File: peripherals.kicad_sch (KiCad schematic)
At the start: 20 parts, among them J10 Cam 2, J11 Cam 3, J13 Servo, J2 Encoder, J9 Cam 1, Q2 NPN, Q3 NPN, Q4 NPN, Q5 NPN

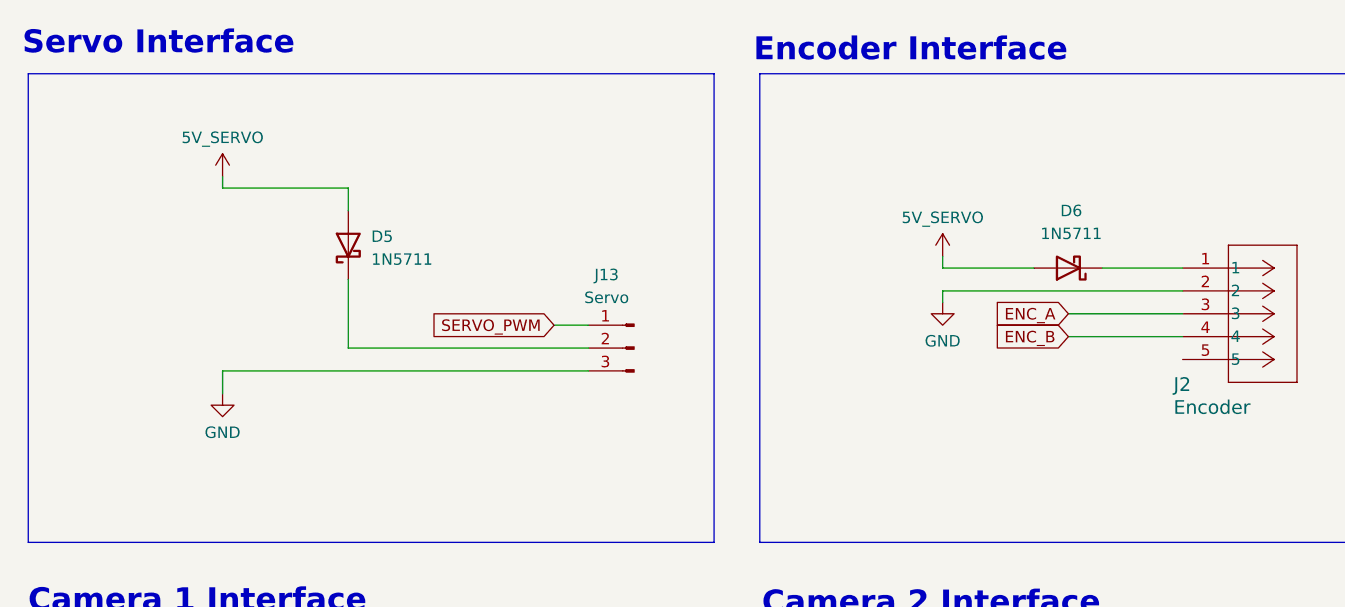
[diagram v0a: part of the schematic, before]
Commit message: remove schotkey diodes from servo and encoder interfaces
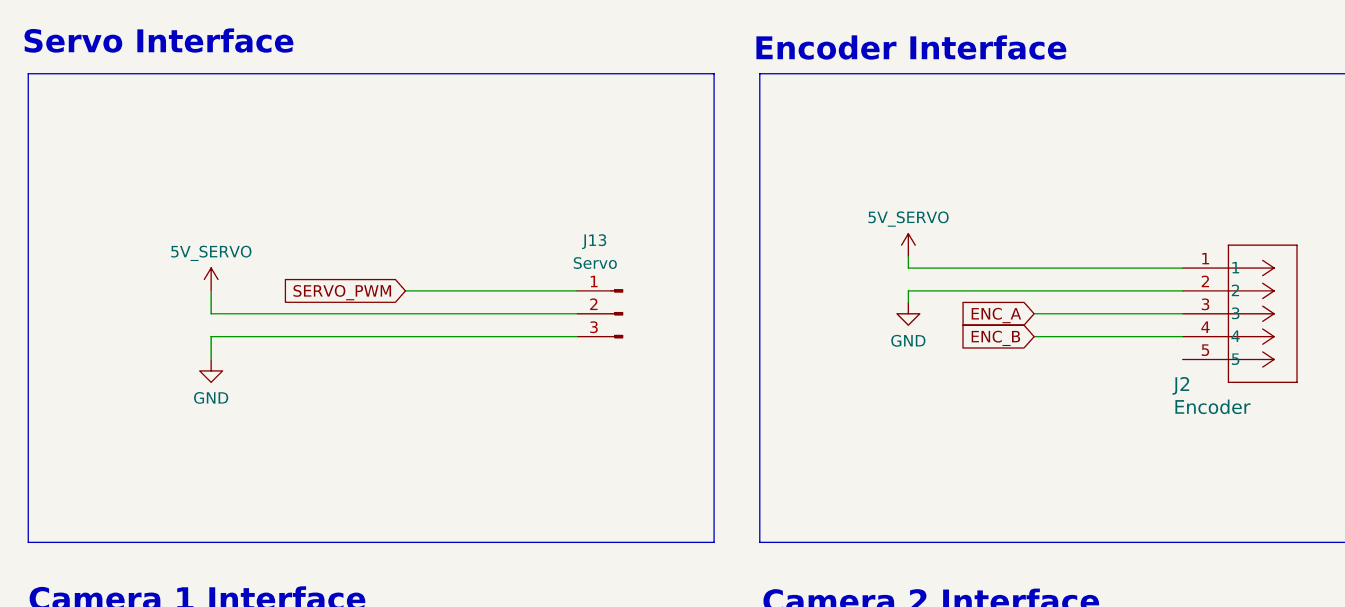
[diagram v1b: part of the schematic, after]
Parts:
- removed D5, D6: 1N5711, Diode_THT:D_DO-35_SOD27_P7.62mm_Horizontal, symbol Diode:1N5711
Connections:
- net 5V_SERVO: now also J13.2 (Pin_2), J2.1
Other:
- moved on the sheet: J13

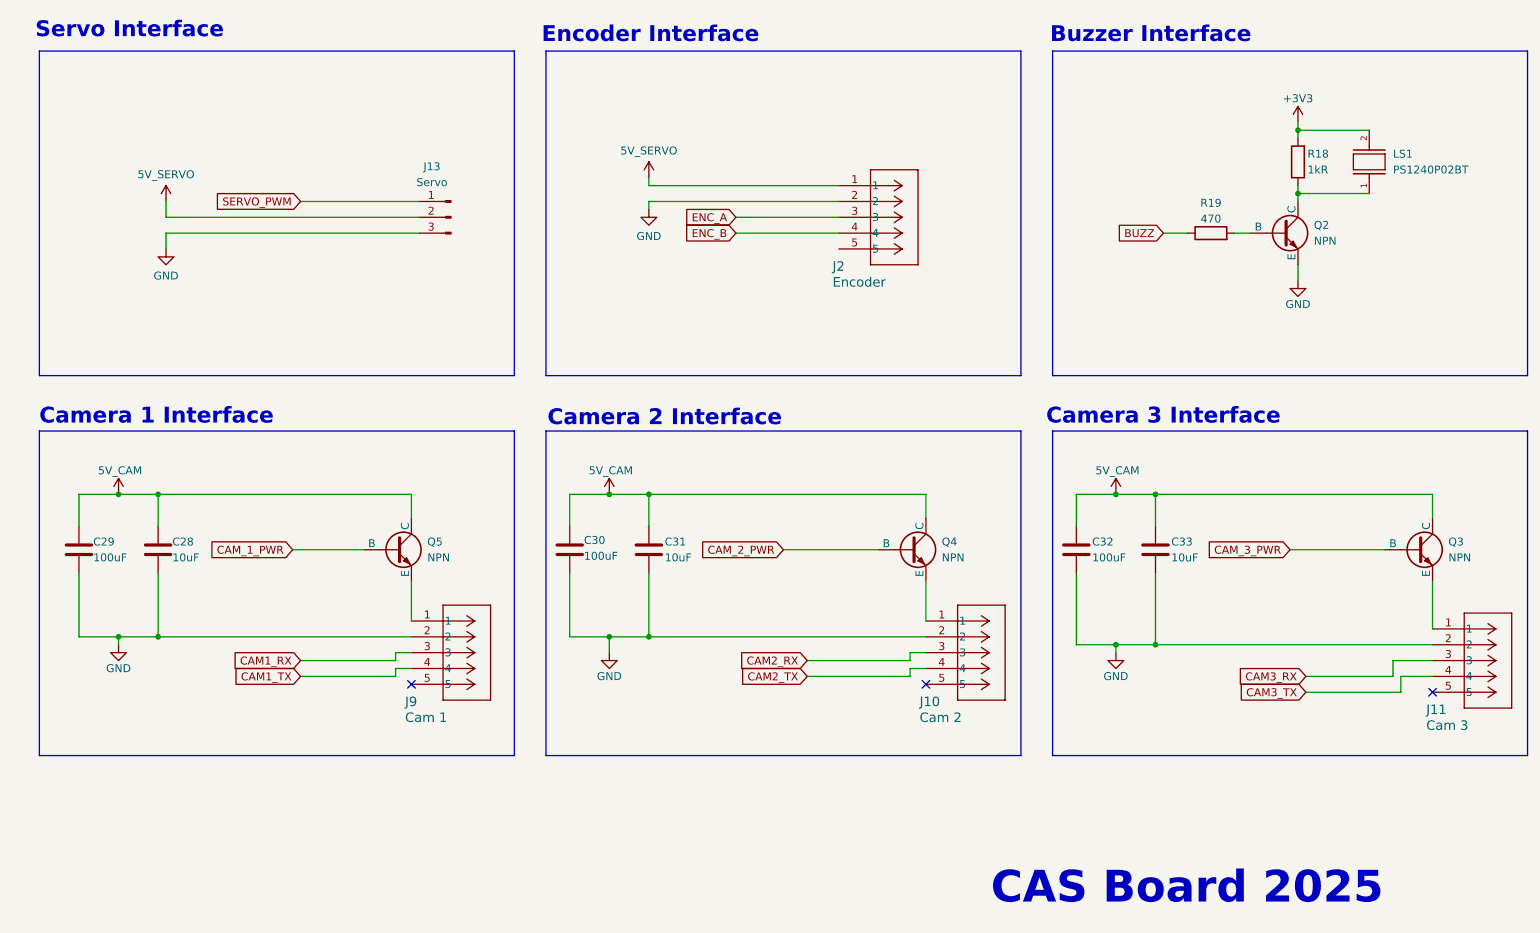
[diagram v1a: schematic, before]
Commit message: Redo footprints and add mosfet for camera power control
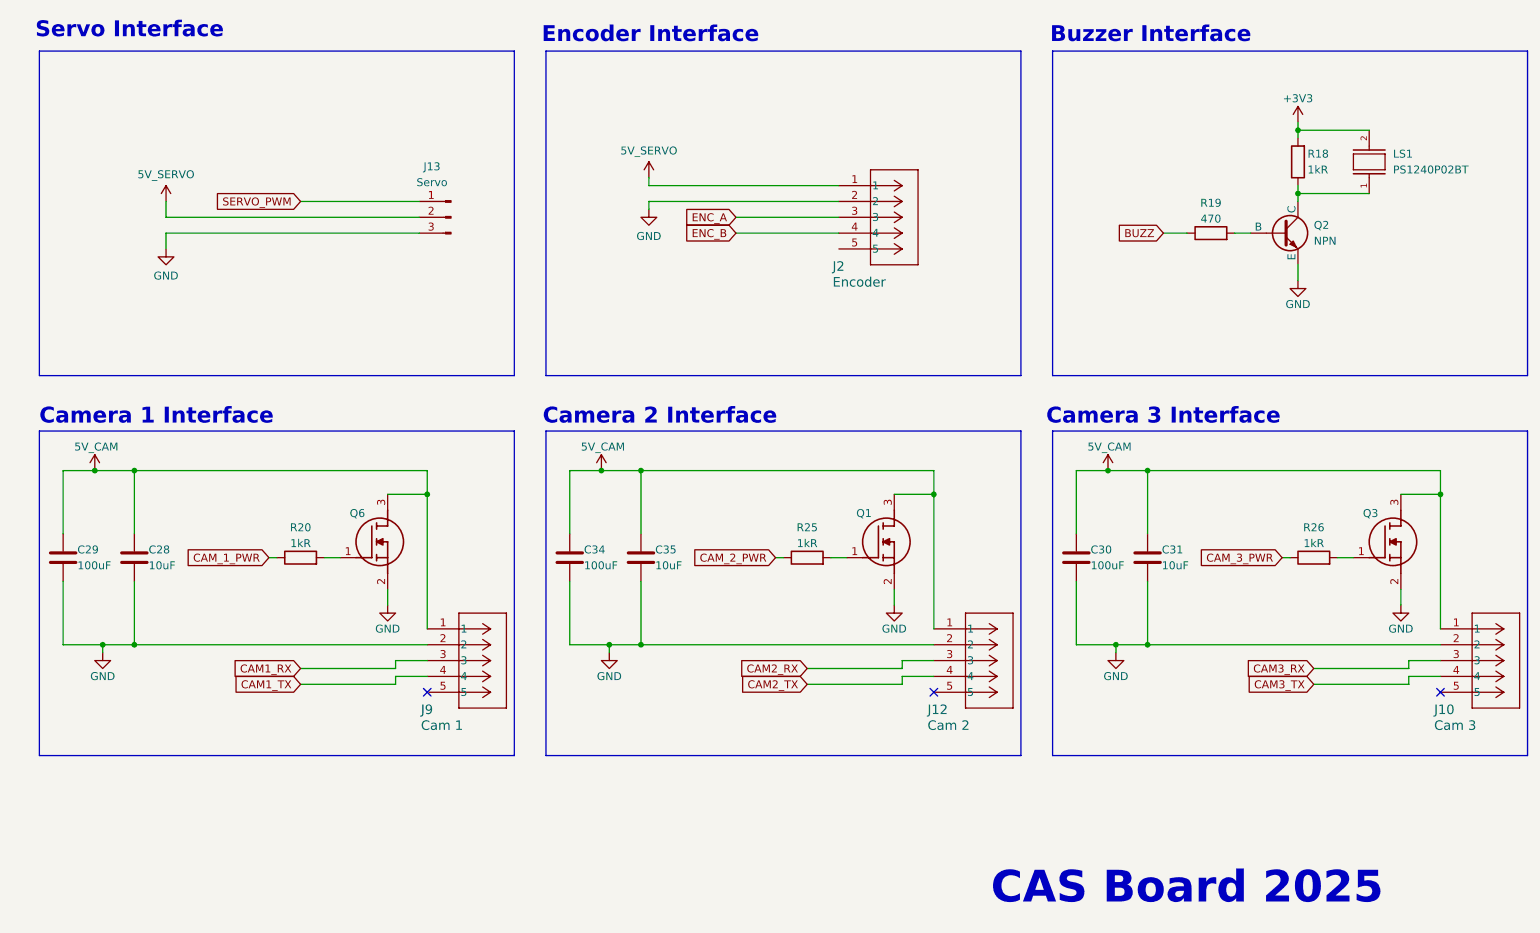
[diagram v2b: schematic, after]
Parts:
- removed C32: 100uF, Capacitor_SMD:C_0805_2012Metric_Pad1.18x1.45mm_HandSolder, symbol Device:C
- removed C33: 10uF, Capacitor_SMD:C_0805_2012Metric_Pad1.18x1.45mm_HandSolder, symbol Device:C
- removed J11: Cam 3, S05B_PASK_2_LF__SN_:CONN_S05B-PASK-2_JST, symbol 2025-06-21_05-21-07:S05B-PASK-2LFSN
- removed Q3, Q4, Q5: NPN, FSB560A:SSOT3_3X1P5_ONS, symbol Simulation_SPICE:NPN
- added C34: 100uF, Capacitor_SMD:C_0805_2012Metric_Pad1.18x1.45mm_HandSolder, symbol Device:C
- added C35: 10uF, Capacitor_SMD:C_0805_2012Metric_Pad1.18x1.45mm_HandSolder, symbol Device:C
- added J12: Cam 2, S05B_PASK_2_LF__SN_:CONN_S05B-PASK-2_JST, symbol 2025-06-21_05-21-07:S05B-PASK-2LFSN
- added Q1, Q3, Q6: BSS816NWH6327XTSA1, SOT65P210X100-3N, symbol BSS816NWH6327XTSA1:BSS816NWH6327XTSA1
- added R20, R25, R26: 1kR, Resistor_SMD:R_0805_2012Metric_Pad1.20x1.40mm_HandSolder, symbol Device:R
- J10: value Cam 2 -> Cam 3
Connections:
- net 5V_CAM: now also J10.1, J9.1, C34.1, C35.1, J12.1, Q1.3 (D), Q3.3 (D), Q6.3 (D)
- net CAM2_RX: now also J12.3; no longer J10.3
- net CAM2_TX: now also J12.4; no longer J10.4
- net CAM3_RX: now also J10.3
- net CAM3_TX: now also J10.4
- net CAM_1_PWR: now also R20.1
- net CAM_2_PWR: now also R25.1
- net CAM_3_PWR: now also R26.1
- net GND: now also C34.2, C35.2, J12.2, Q1.2 (S), Q3.2 (S), Q6.2 (S)
- new net: Q6.1 (G), R20.2
- new net: Q1.1 (G), R25.2
- new net: Q3.1 (G), R26.2
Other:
- moved on the sheet: C28, C29, J9

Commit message: Use heirarchical labels
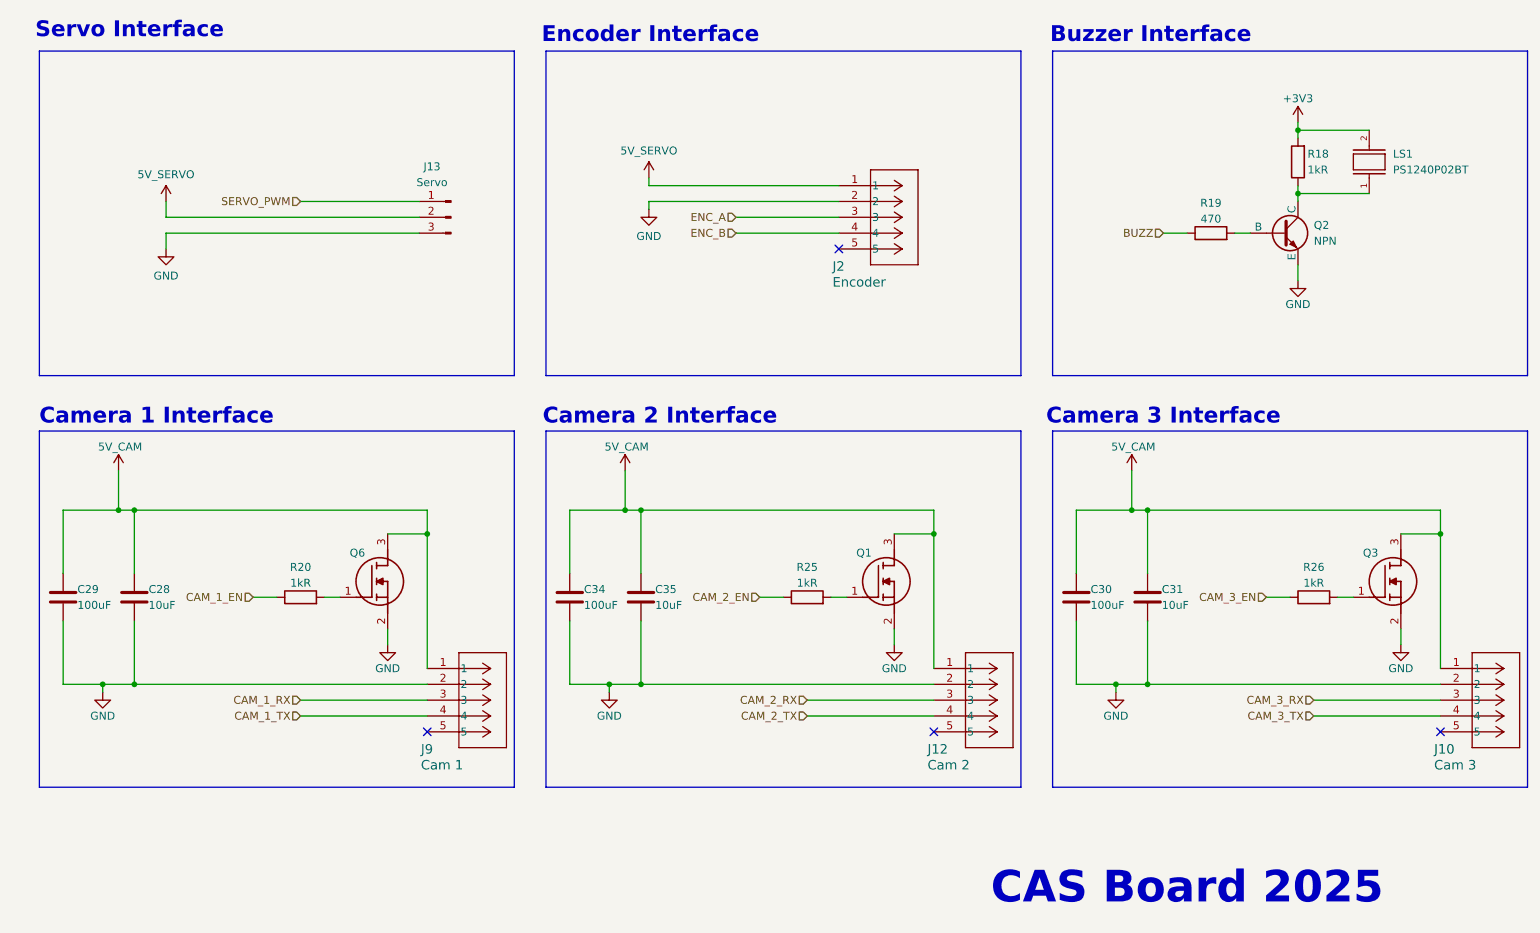
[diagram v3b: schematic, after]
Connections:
- net CAM1_RX renamed CAM_1_RX
- net CAM1_TX renamed CAM_1_TX
- net CAM2_RX renamed CAM_2_RX
- net CAM2_TX renamed CAM_2_TX
- net CAM3_RX renamed CAM_3_RX
- net CAM3_TX renamed CAM_3_TX
- net CAM_1_PWR renamed CAM_1_EN
- net CAM_2_PWR renamed CAM_2_EN
- net CAM_3_PWR renamed CAM_3_EN
- no-connect marks 3 -> 4
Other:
- moved on the sheet: C28, C29, C30, C31, C34, C35, J10, J12, J9, Q1, Q3, Q6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

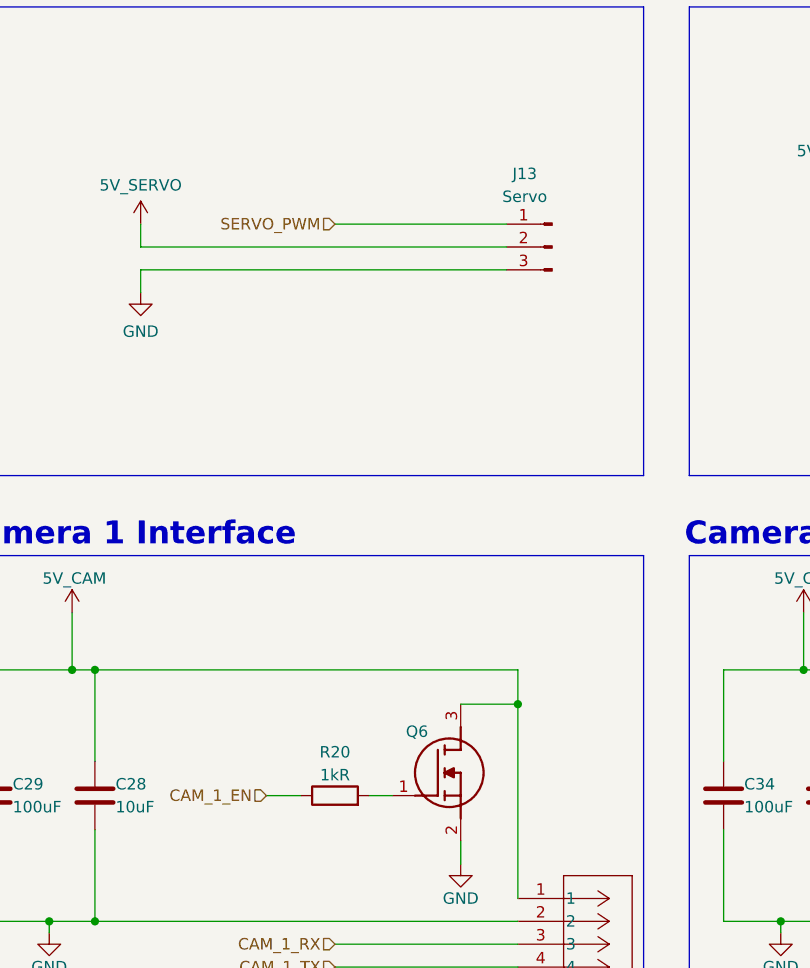
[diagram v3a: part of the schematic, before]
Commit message: Broke headers into own heiarchicial sheet
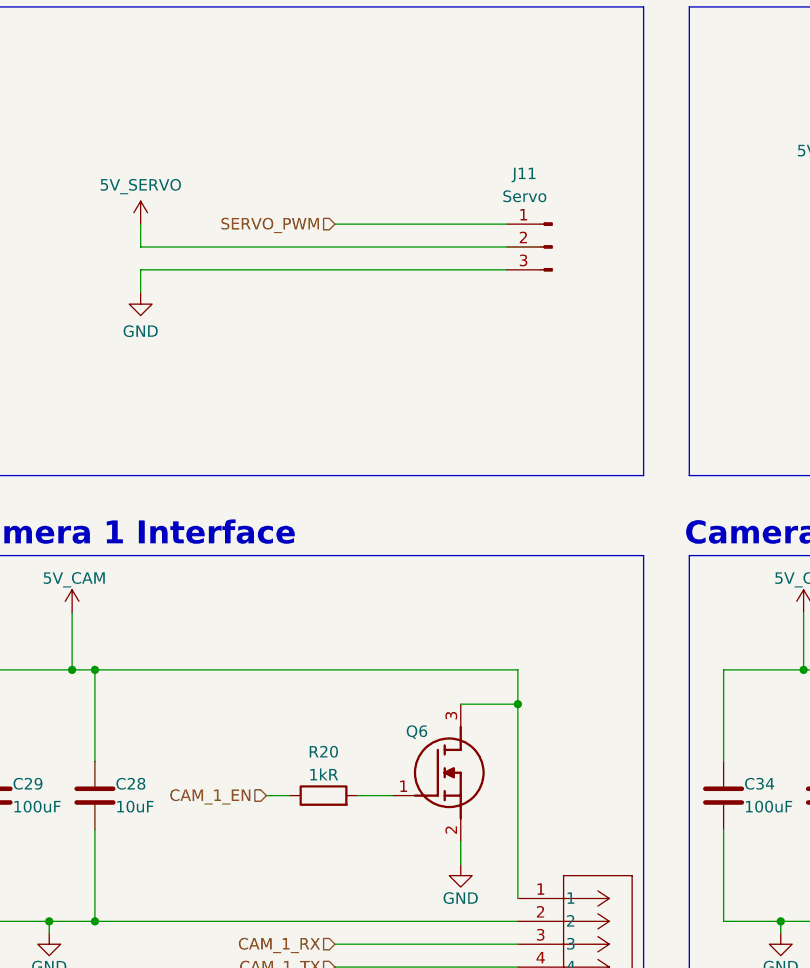
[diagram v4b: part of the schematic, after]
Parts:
- Q6: footprint SOT65P210X100-3N -> BSS816NWH6327XTSA1:SOT65P210X100-3N
- renumbered J13 to J11
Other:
- moved on the sheet: R20
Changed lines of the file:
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@@
 	(wire
 		(pts
-			(xy 59.69 127) (xy 63.5 127)
+			(xy 59.69 127) (xy 62.23 127)
 		)
 		(stroke
@@
 	(wire
 		(pts
+			(xy 69.85 127) (xy 73.66 127)
+		)
+		(stroke
+			(width 0)
+			(type default)
+		)
+	)
+	(wire
+		(pts
 			(xy 229.87 143.51) (xy 250.19 143.51)
 		)
@@
 	(wire
 		(pts
-			(xy 71.12 127) (xy 73.66 127)
-		)
-		(stroke
-			(width 0)
-			(type default)
-		)
-	)
-	(wire
-		(pts
 			(xy 227.33 52.07) (xy 238.76 52.07)
 		)
@@
 	(symbol
 		(lib_id "Device:R")
-		(at 67.31 127 90)
+		(at 66.04 127 90)
 		(unit 1)
 		(exclude_from_sim no)
@@
 		(dnp no)
 		(property "Reference" "R20"
-			(at 67.31 122.174 90)
+			(at 66.04 122.174 90)
 			(effects
 				(font
@@
 		)
 		(property "Value" "1kR"
-			(at 67.31 124.714 90)
+			(at 66.04 124.714 90)
 			(effects
 				(font
@@
 		)
 		(property "Footprint" "Resistor_SMD:R_0805_2012Metric_Pad1.20x1.40mm_HandSolder"
-			(at 67.31 128.778 90)
+			(at 66.04 128.778 90)
 			(effects
 				(font
@@
 		)
 		(property "Datasheet" "~"
-			(at 67.31 127 0)
+			(at 66.04 127 0)
 			(effects
 				(font
@@
 		)
 		(property "Description" "Resistor"
-			(at 67.31 127 0)
+			(at 66.04 127 0)
 			(effects
 				(font
@@
 		)
 		(instances
-			(project ""
+			(project "SimplerFlight_v2"
 				(path "/05521696-5bcb-4d0e-9e87-bbc993e58ce4/48646a32-6556-4772-9e6c-3c45575ecce9"
 					(reference "R20")
@@
 		)
 		(instances
-			(project ""
+			(project "SimplerFlight_v2"
 				(path "/05521696-5bcb-4d0e-9e87-bbc993e58ce4/48646a32-6556-4772-9e6c-3c45575ecce9"
 					(reference "LS1")
@@
 		)
 		(instances
-			(project ""
+			(project "SimplerFlight_v2"
 				(path "/05521696-5bcb-4d0e-9e87-bbc993e58ce4/48646a32-6556-4772-9e6c-3c45575ecce9"
 					(reference "Q2")
@@
 			)
 		)
-		(property "Footprint" "SOT65P210X100-3N"
+		(property "Footprint" "BSS816NWH6327XTSA1:SOT65P210X100-3N"
 			(at 85.09 225.73 0)
 			(effects
@@
 		(on_board yes)
 		(dnp no)
-		(property "Reference" "J13"
+		(property "Reference" "J11"
 			(at 88.392 57.912 0)
 			(effects
@@
 		)
 		(instances
-			(project ""
+			(project "SimplerFlight_v2"
 				(path "/05521696-5bcb-4d0e-9e87-bbc993e58ce4/48646a32-6556-4772-9e6c-3c45575ecce9"
-					(reference "J13")
+					(reference "J11")
 					(unit 1)
 				)
@@
 		)
 		(instances
-			(project ""
+			(project "SimplerFlight_v2"
 				(path "/05521696-5bcb-4d0e-9e87-bbc993e58ce4/48646a32-6556-4772-9e6c-3c45575ecce9"
 					(reference "C28")
